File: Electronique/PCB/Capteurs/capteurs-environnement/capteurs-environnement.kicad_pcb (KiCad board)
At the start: 2 copper layers, 87.6 x 62.2 mm, 12 parts, among them U1 Pico, U2 STEMMA, U3 STEMMA, U4 STEMMA

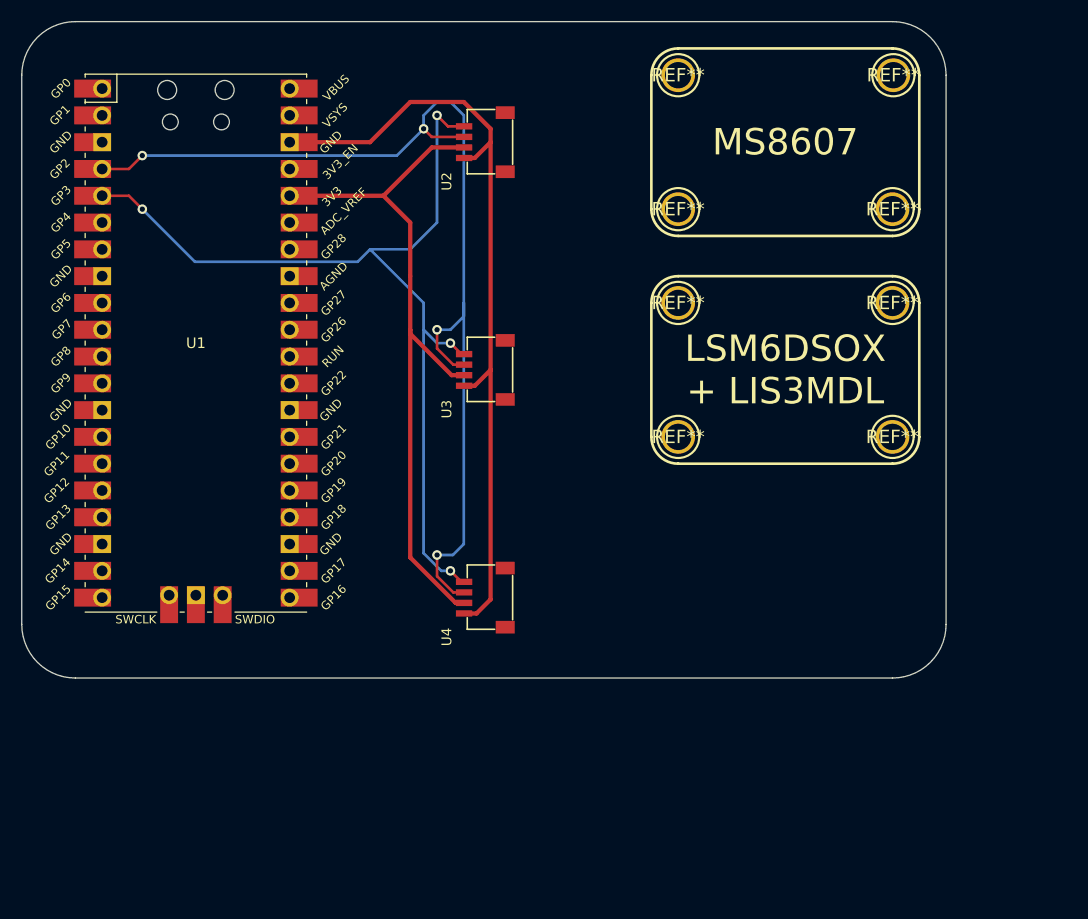
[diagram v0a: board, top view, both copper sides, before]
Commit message: update to pcb for environnement sensors + external libs
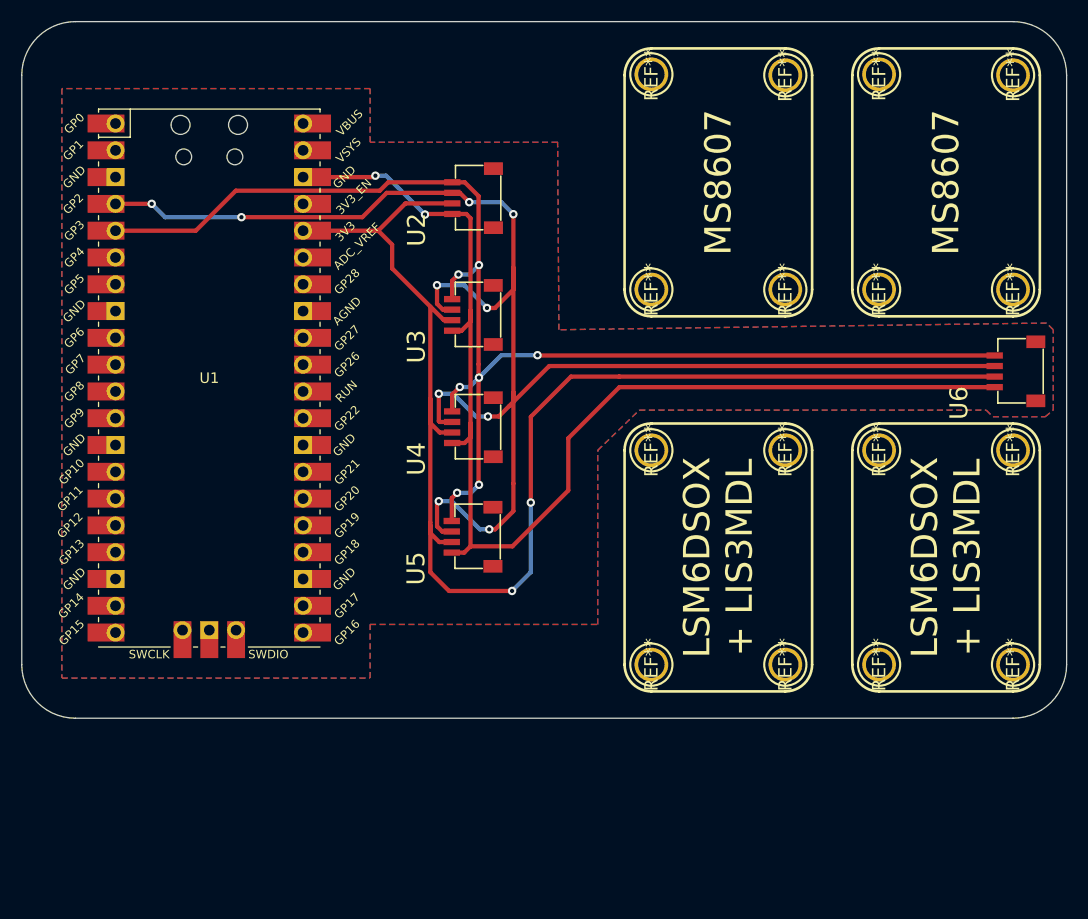
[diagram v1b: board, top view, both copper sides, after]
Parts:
- added REF**: , Adafruit MS8607:MOUNTINGHOLE_2.5_PLATED, F.Cu at (158.8, 121.9)
- added REF**: , Adafruit MS8607:MOUNTINGHOLE_2.5_PLATED, F.Cu at (146.1, 86.4)
- added REF**: , Adafruit MS8607:MOUNTINGHOLE_2.5_PLATED, F.Cu at (158.8, 66.0)
- added REF**: , Adafruit MS8607:MOUNTINGHOLE_2.5_PLATED, F.Cu at (146.1, 121.9)
- added REF**: , Adafruit MS8607:MOUNTINGHOLE_2.5_PLATED, F.Cu at (158.8, 86.4)
- added REF**: , Adafruit MS8607:MOUNTINGHOLE_2.5_PLATED, F.Cu at (146.1, 101.6)
- added REF**: , Adafruit MS8607:MOUNTINGHOLE_2.5_PLATED, F.Cu at (146.1, 66.0)
- added REF**: , Adafruit MS8607:MOUNTINGHOLE_2.5_PLATED, F.Cu at (158.8, 101.6)
- added U5: ~, Connectors:JST_SH4, F.Cu at (108.1, 109.8)
- added U6: ~, Connectors:JST_SH4, F.Cu at (159.5, 94.1)
- U2, U3, U4: value STEMMA -> ~; footprint Adafruit MS8607:JST_SH4 -> Connectors:JST_SH4
- moved REF** 34.4 mm to (124.5, 121.9), turned to 90 degrees
- moved REF** 26.8 mm to (124.5, 101.6), turned to 90 degrees
- moved REF** 23.9 mm to (137.2, 121.9), turned to 90 degrees
- moved REF** 22.9 mm to (124.5, 66.0), turned to 90 degrees
- moved REF** 20.5 mm to (124.5, 86.4), turned to 90 degrees
- moved REF** 16.3 mm to (137.2, 66.0), turned to 90 degrees
- moved U4 16.2 mm to (108.1, 99.4)
- moved REF** 12.7 mm to (137.2, 86.4), turned to 90 degrees
- moved REF** 10.2 mm to (137.2, 101.6), turned to 90 degrees
- moved U2 5.42 mm to (108.1, 77.7)
- moved U3 5.33 mm to (108.1, 88.8)
- moved U1 3.55 mm to (82.5, 94.8)
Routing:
- net +3.3V: track 67.8 -> 131.4 mm, vias 0 -> 2
- net /SDA: track 100.2 -> 155.9 mm, vias 4 -> 10
- net GND: track 75.6 -> 116.2 mm, vias 0 -> 2
- net /SCL: track 89.7 -> 129.0 mm, vias 4 -> 7
- added copper zone on B.Cu, net GND
- added copper zone on F.Cu, net GND
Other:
- board size 87.6 x 62.2 mm -> 99.1 x 66 mm

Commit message: pcb updates
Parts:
- moved U6 63.4 mm to (110.7, 134.6), turned to 0 degrees
- moved U4 44.5 mm to (152.4, 95.1), turned to 0 degrees
- moved U5 44.3 mm to (152.4, 110.2), turned to 180 degrees
- moved U3 31.3 mm to (130.8, 110.2), turned to 180 degrees
- moved U2 28.5 mm to (130.8, 95.0), turned to 0 degrees
- moved REF** 17.1 mm to (137.0, 139.0)
- moved REF** 17.1 mm to (158.6, 139.0)
- moved REF** 17.1 mm to (124.3, 118.7)
- moved REF** 17.1 mm to (137.0, 118.7)
- moved REF** 17.1 mm to (145.9, 139.0)
- moved REF** 17.1 mm to (124.3, 139.0)
- moved REF** 17.1 mm to (145.9, 118.7)
- moved REF** 17.1 mm to (158.6, 118.7)
- moved U1 7.84 mm to (86.4, 101.6)
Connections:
- U2 pad MT1: GND -> unconnected-(U2-PadMT1)
- U2 pad MT2: GND -> unconnected-(U2-PadMT2)
- U3 pad MT1: GND -> unconnected-(U3-PadMT1)
- U3 pad MT2: GND -> unconnected-(U3-PadMT2)
- U4 pad MT1: GND -> unconnected-(U4-PadMT1)
- U4 pad MT2: GND -> unconnected-(U4-PadMT2)
- U5 pad MT1: GND -> unconnected-(U5-PadMT1)
- U5 pad MT2: GND -> unconnected-(U5-PadMT2)
- U6 pad MT1: GND -> unconnected-(U6-PadMT1)
- U6 pad MT2: GND -> unconnected-(U6-PadMT2)
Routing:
- net GND: track 116.2 -> 150.5 mm, vias 2 -> 4
- net /SCL: track 129.0 -> 162.1 mm, vias 7 -> 6
- net +3.3V: track 131.4 -> 145.1 mm, vias 2 -> 8
- net /SDA: track 155.9 -> 163.3 mm, vias 10 -> 8
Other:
- board size 99.1 x 66 mm -> 99.1 x 83 mm
- board text added: "Pico watchdog for 9 dof IMU and environnement sensors"
